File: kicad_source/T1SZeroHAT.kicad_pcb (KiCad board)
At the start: 2 copper layers, 65 x 30 mm, 44 parts, among them CN1 RASPI-IO, CN2 XY2500R-F-3.81-2P, CN3 SM02B-GHS-TB, CN4 SM02B-GHS-TB, SW1 SS-3235S-L3, U1 LAN8651, Y1 X1E0000210808

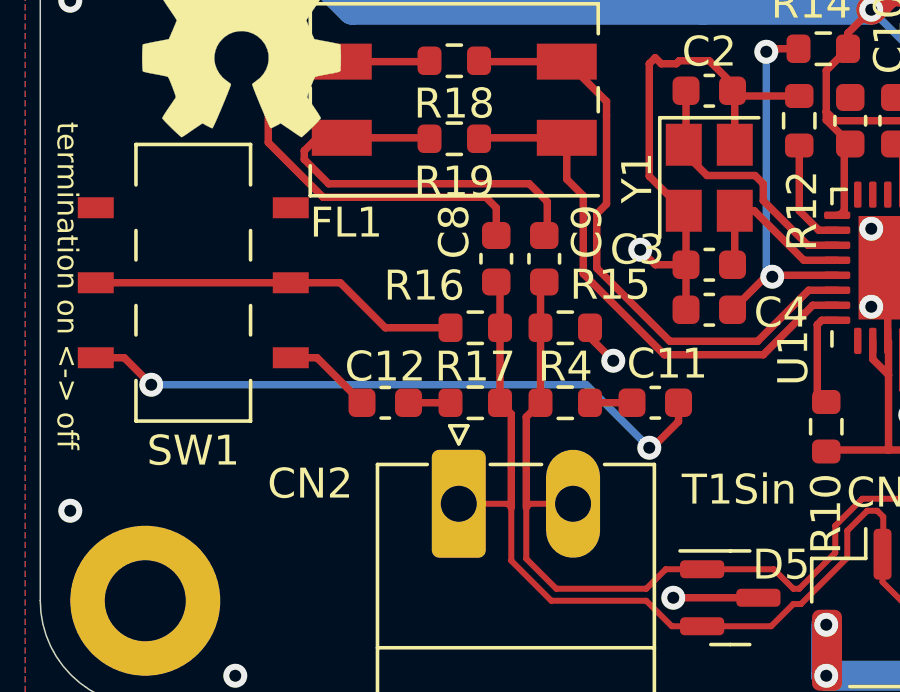
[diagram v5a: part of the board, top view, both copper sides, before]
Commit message: changed R14..R17 to 1206 according to microchip reference schematic
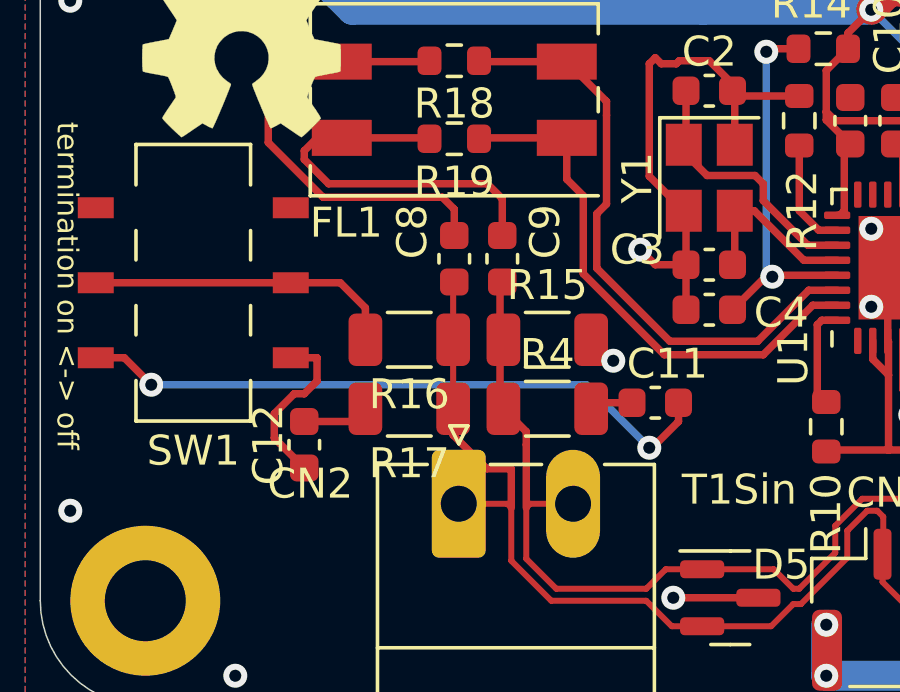
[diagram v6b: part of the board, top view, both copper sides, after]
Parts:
- R15, R16, R17, R4: footprint Resistor_SMD:R_0603_1608Metric -> Resistor_SMD:R_1206_3216Metric
- moved C12 3.04 mm to (116.3, 107.8), turned to -90 degrees
- moved R16 2.24 mm to (119.8, 104.3)
- moved R17 2.21 mm to (119.8, 106.6)
- moved C8 1.40 mm to (121.3, 101.6)
- moved C9 1.40 mm to (122.9, 101.6)
- moved R15 0.72 mm to (124.4, 104.3)
- moved R4 0.63 mm to (124.4, 106.6)
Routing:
- net Net-(SW1B-A): track 3.00 -> 5.75 mm
- net GND: track 111.5 -> 109.4 mm
- net /TRXN_I: track 14.5 -> 13.0 mm
- net /TRXP_I: track 17.1 -> 15.6 mm
- net /TRXP: track 38.9 -> 40.0 mm
- net Net-(C12-Pad1): track 1.40 -> 2.21 mm

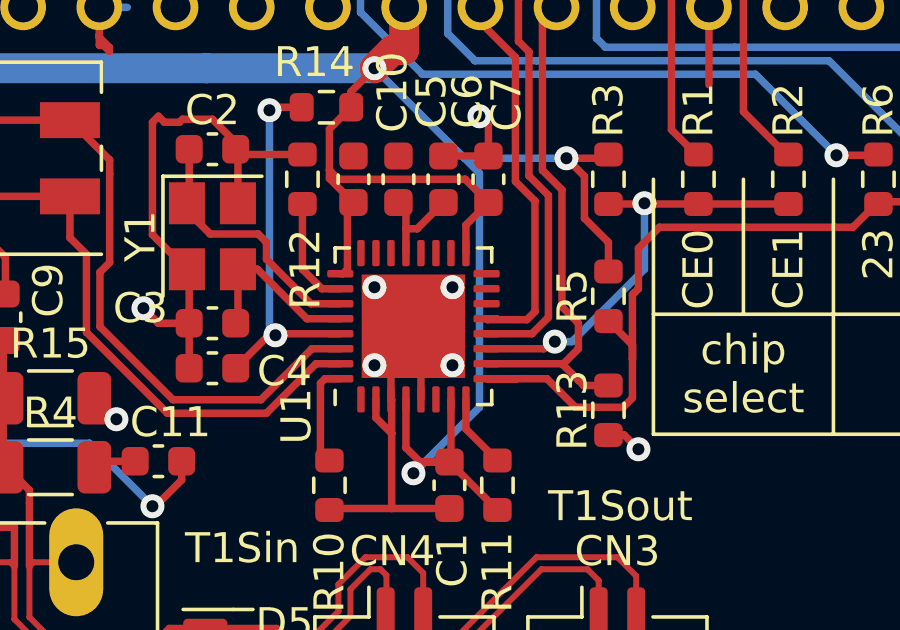
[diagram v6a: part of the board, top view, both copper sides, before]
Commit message: connected DIOB1 directly to GND as recommended in datasheet
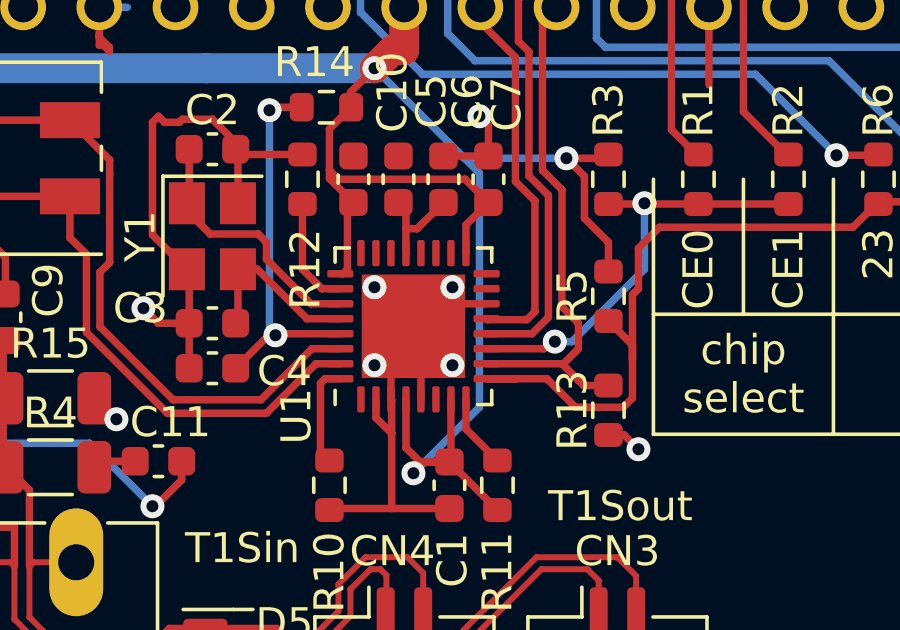
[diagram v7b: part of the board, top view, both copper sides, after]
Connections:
- U1 pad 14: unconnected-(U1-DIOB1-Pad14) -> GND
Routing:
- net GND: track 109.4 -> 112.2 mm
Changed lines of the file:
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@@
 	(net 61 "unconnected-(U1-WAKE_OUT-Pad24)")
 	(net 62 "unconnected-(U1-DNC-Pad15)")
-	(net 63 "unconnected-(U1-DIOB1-Pad14)")
-	(net 64 "/CCOMP")
+	(net 63 "/CCOMP")
 	(footprint "Capacitor_SMD:C_0603_1608Metric"
 		(layer "F.Cu")
@@
 			(layers "F.Cu" "F.Paste" "F.Mask")
 			(roundrect_rratio 0.25)
-			(net 63 "unconnected-(U1-DIOB1-Pad14)")
+			(net 3 "GND")
 			(pinfunction "DIOB1")
-			(pintype "input+no_connect")
+			(pintype "input")
 		)
 		(pad "15" smd roundrect
@@
 			(layers "F.Cu" "F.Paste" "F.Mask")
 			(roundrect_rratio 0.25)
-			(net 64 "/CCOMP")
+			(net 63 "/CCOMP")
 			(pinfunction "CCOMP")
 			(pintype "input")
@@
 			(layers "F.Cu" "F.Paste" "F.Mask")
 			(roundrect_rratio 0.25)
-			(net 64 "/CCOMP")
+			(net 63 "/CCOMP")
 			(pintype "passive")
 		)
@@
 			(layers "F.Cu" "F.Paste" "F.Mask")
 			(roundrect_rratio 0.25)
-			(net 64 "/CCOMP")
+			(net 63 "/CCOMP")
 			(pintype "passive")
 		)
@@
 	)
 	(segment
+		(start 137.25 101.15)
+		(end 136.5 101.9)
+		(width 0.25)
+		(layer "F.Cu")
+		(net 3)
+	)
+	(segment
 		(start 130.575 96)
 		(end 130.575 95.775)
@@
 	)
 	(segment
+		(start 138.9375 101.15)
+		(end 137.25 101.15)
+		(width 0.25)
+		(layer "F.Cu")
+		(net 3)
+	)
+	(segment
 		(start 126.03 91.27)
 		(end 127.482999 89.817001)
@@
 		(width 0.25)
 		(layer "F.Cu")
-		(net 64)
+		(net 63)
 	)
 	(segment
@@
 		(width 0.25)
 		(layer "F.Cu")
-		(net 64)
+		(net 63)
 	)
 	(segment
@@
 		(width 0.25)
 		(layer "F.Cu")
-		(net 64)
+		(net 63)
 	)
 	(segment
@@
 		(width 0.25)
 		(layer "F.Cu")
-		(net 64)
+		(net 63)
 	)
 	(segment
@@
 		(width 0.25)
 		(layer "F.Cu")
-		(net 64)
+		(net 63)
 	)
 	(zone

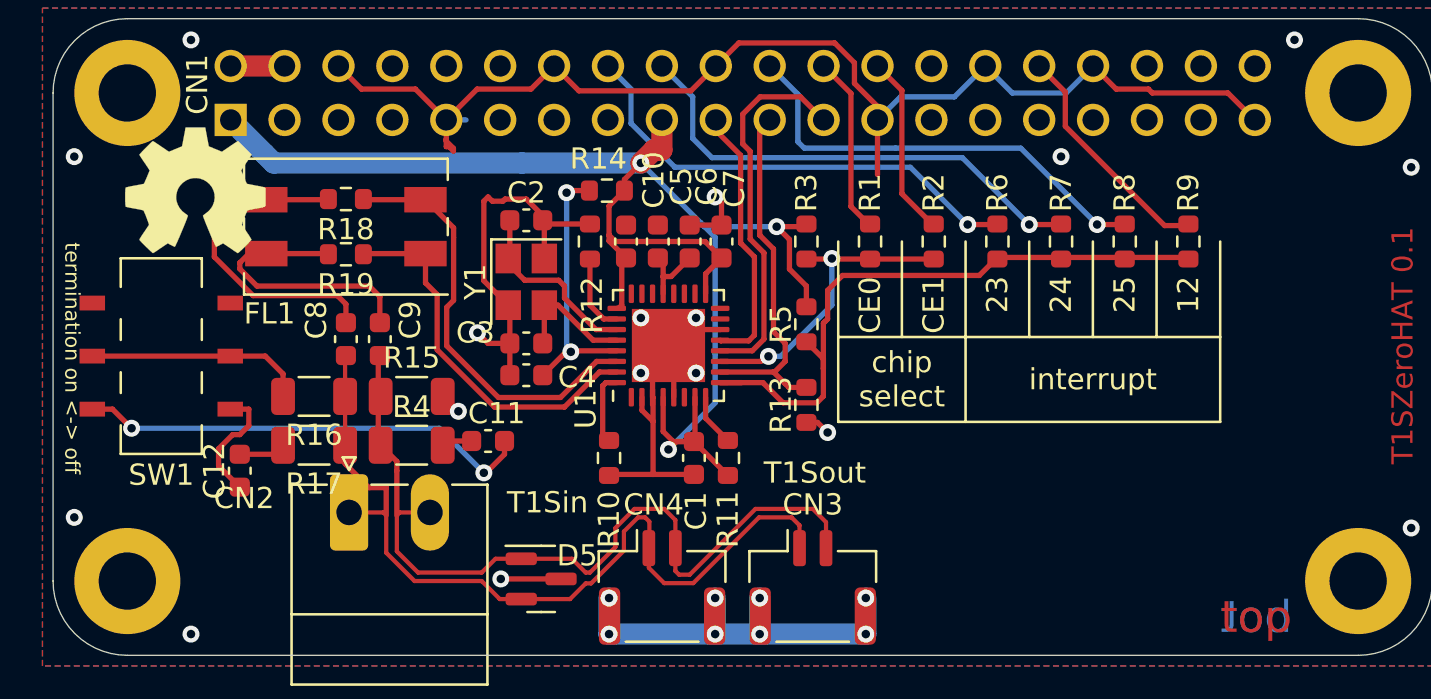
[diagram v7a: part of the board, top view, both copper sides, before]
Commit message: reworked power part
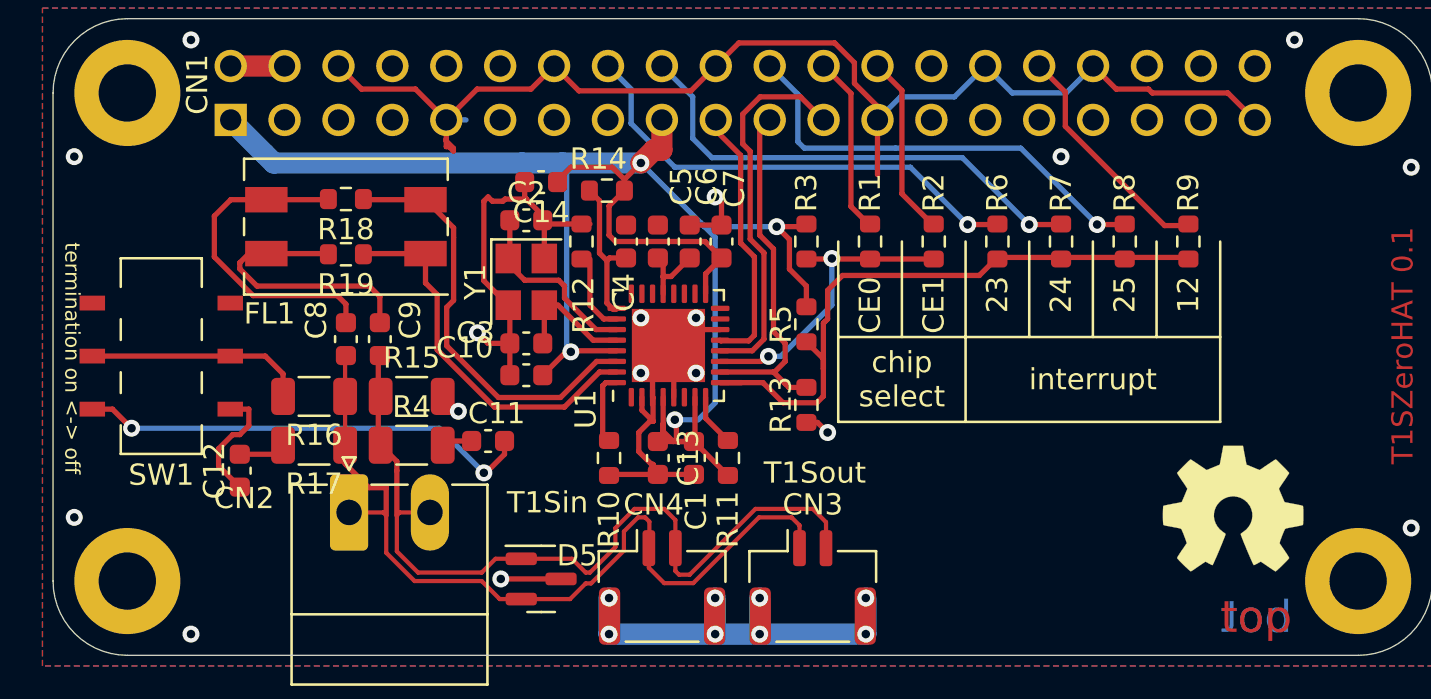
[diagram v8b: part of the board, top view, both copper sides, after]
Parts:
- removed L4: Label, generationmake:opencyphal_small
- added C13: 10 uF, Capacitor_SMD:C_0603_1608Metric, F.Cu at (136.0, 107.2)
- added C14: 10 uF, Capacitor_SMD:C_0603_1608Metric, F.Cu at (130.5, 94.2)
- moved L3 51.1 mm to (163.1, 109.6)
- moved C10 7.86 mm to (129.8, 103.3), turned to 180 degrees
- moved C4 7.86 mm to (134.5, 97.0), turned to 90 degrees
- moved R12 0.40 mm to (132.4, 97.0)
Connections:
- C4 pad 1: /VDDA -> /VDDAU
- R14 pad 2: /VDDA -> /VDDAU
- U1 pad 25: +3.3V -> /VDDAU
- U1 pad 29: /VDDA -> +3.3V
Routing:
- net +3.3V: track 73.0 -> 87.2 mm, vias 3 -> 4
- net /VDDA: track 12.8 -> 0.00 mm, vias 2 -> 0
- net /VDDAU: track 0.00 -> 7.57 mm
- net GND: track 112.2 -> 113.7 mm
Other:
- board text added: "for Microchip LAN8651"
- board text removed: "for Microchip MCP2517FD or MCP2518FD"
